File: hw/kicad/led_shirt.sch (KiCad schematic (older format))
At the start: 23 parts, among them J1 10103593-0001LF, P1 icpc, P2 icpd, P3 gnd, P4 v+, P5 mclr, P6 bat+, P7 bat-, P8 led1-, P9 led1+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

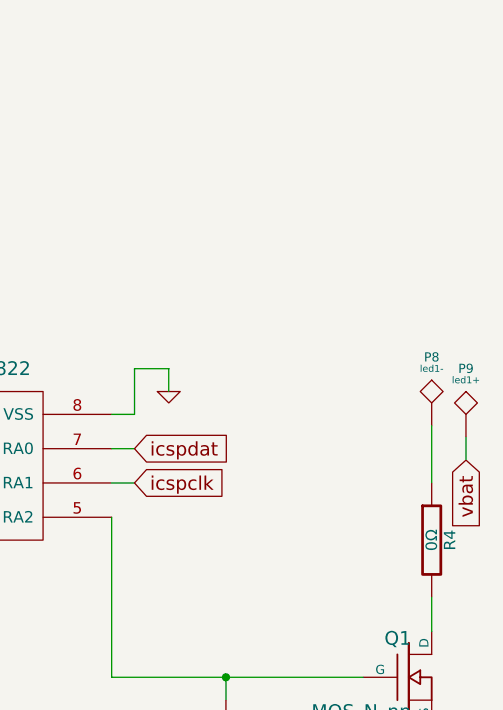
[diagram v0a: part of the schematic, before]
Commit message: add leds to onboard
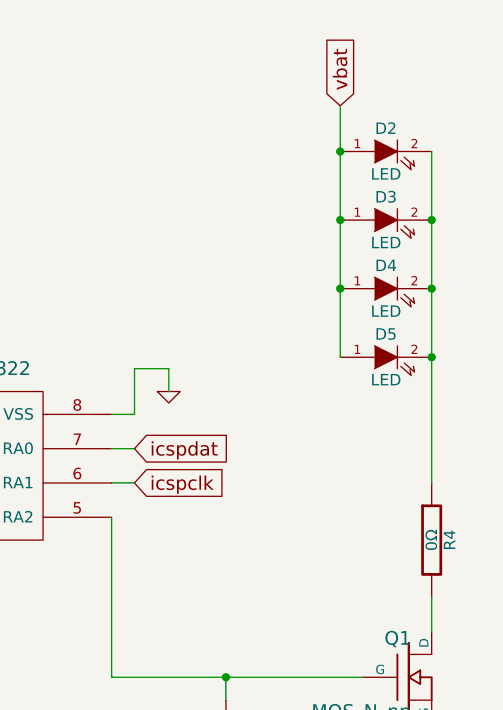
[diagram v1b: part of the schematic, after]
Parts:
- removed P8: led1-, symbol TST
- removed P9: led1+, symbol TST
- added D2, D3, D4, D5: LED, symbol LED
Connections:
- net vbat: now also D2.1 (A), D3.1 (A), D4.1 (A), D5.1 (A)
- net at R4.1: now also D2.2 (K), D3.2 (K), D4.2 (K), D5.2 (K)
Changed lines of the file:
@@
 LIBS:extra
 LIBS:led_shirt-cache
-EELAYER 27 0
+EELAYER 24 0
 EELAYER END
 $Descr A4 11693 8268
@@
 Comment4 ""
 $EndDescr
-Text GLabel 8750 2700 3    60   Input ~ 0
+Text GLabel 8200 1150 1    60   Input ~ 0
 vbat
 $Comp
@@
 	1    0    0    -1
 $EndComp
-$Comp
-L TST P8
-U 1 1 50A3E96A
-P 8600 2550
-F 0 "P8" H 8600 2850 40  0000 C CNN
-F 1 "led1-" H 8600 2800 30  0000 C CNN
-F 2 "" H 8600 2550 60  0001 C CNN
-F 3 "" H 8600 2550 60  0001 C CNN
-	1    8600 2550
-	1    0    0    -1
-$EndComp
 Text GLabel 5450 1900 0    60   Input ~ 0
 vbat
@@
 $EndComp
 $Comp
-L GND #PWR01
+L GND #PWR5
 U 1 1 509FF06B
 P 4650 2700
-F 0 "#PWR01" H 4650 2700 30  0001 C CNN
+F 0 "#PWR5" H 4650 2700 30  0001 C CNN
 F 1 "GND" H 4650 2630 30  0001 C CNN
 F 2 "" H 4650 2700 60  0001 C CNN
@@
 $EndComp
 $Comp
-L TST P9
-U 1 1 509ED371
-P 8750 2600
-F 0 "P9" H 8750 2900 40  0000 C CNN
-F 1 "led1+" H 8750 2850 30  0000 C CNN
-F 2 "" H 8750 2600 60  0001 C CNN
-F 3 "" H 8750 2600 60  0001 C CNN
-	1    8750 2600
-	1    0    0    -1
-$EndComp
-$Comp
 L R R4
 U 1 1 509E9C0F
@@
 $EndComp
 $Comp
-L GND #PWR02
+L GND #PWR2
 U 1 1 509D17CA
 P 2450 3450
-F 0 "#PWR02" H 2450 3450 30  0001 C CNN
+F 0 "#PWR2" H 2450 3450 30  0001 C CNN
 F 1 "GND" H 2450 3380 30  0001 C CNN
 F 2 "" H 2450 3450 60  0001 C CNN
@@
 $EndComp
 $Comp
-L GND #PWR03
+L GND #PWR4
 U 1 1 509D14DE
 P 3250 1650
-F 0 "#PWR03" H 3250 1650 30  0001 C CNN
+F 0 "#PWR4" H 3250 1650 30  0001 C CNN
 F 1 "GND" H 3250 1580 30  0001 C CNN
 F 2 "" H 3250 1650 60  0001 C CNN
@@
 $EndComp
 $Comp
-L GND #PWR04
+L GND #PWR7
 U 1 1 509D02E2
 P 7450 2400
-F 0 "#PWR04" H 7450 2400 30  0001 C CNN
+F 0 "#PWR7" H 7450 2400 30  0001 C CNN
 F 1 "GND" H 7450 2330 30  0001 C CNN
 F 2 "" H 7450 2400 60  0001 C CNN
@@
 vbat
 $Comp
-L GND #PWR05
+L GND #PWR6
 U 1 1 509D029F
 P 4900 6150
-F 0 "#PWR05" H 4900 6150 30  0001 C CNN
+F 0 "#PWR6" H 4900 6150 30  0001 C CNN
 F 1 "GND" H 4900 6080 30  0001 C CNN
 F 2 "" H 4900 6150 60  0001 C CNN
@@
 $EndComp
 $Comp
-L GND #PWR06
+L GND #PWR3
 U 1 1 509D017A
 P 2450 5850
-F 0 "#PWR06" H 2450 5850 30  0001 C CNN
+F 0 "#PWR3" H 2450 5850 30  0001 C CNN
 F 1 "GND" H 2450 5780 30  0001 C CNN
 F 2 "" H 2450 5850 60  0001 C CNN
@@
 vbus
 $Comp
-L GND #PWR07
+L GND #PWR1
 U 1 1 509D0101
 P 1800 1850
-F 0 "#PWR07" H 1800 1850 30  0001 C CNN
+F 0 "#PWR1" H 1800 1850 30  0001 C CNN
 F 1 "GND" H 1800 1780 30  0001 C CNN
 F 2 "" H 1800 1850 60  0001 C CNN
@@
 $EndComp
 $Comp
-L GND #PWR08
+L GND #PWR8
 U 1 1 52607FD1
 P 8150 4500
-F 0 "#PWR08" H 8150 4500 30  0001 C CNN
+F 0 "#PWR8" H 8150 4500 30  0001 C CNN
 F 1 "GND" H 8150 4430 30  0001 C CNN
 F 2 "" H 8150 4500 60  0000 C CNN
@@
 $EndComp
 Wire Wire Line
-	8750 2600 8750 2700
-Wire Wire Line
 	5450 1900 5450 2050
 Wire Wire Line
@@
 Wire Wire Line
 	8600 3450 8600 3300
-Wire Wire Line
-	8600 2550 8600 2800
 Wire Wire Line
 	5350 2650 6000 2650
@@
 	8600 4400 8600 3850
 Connection ~ 8150 4400
+$Comp
+L LED D2
+U 1 1 526D96FC
+P 8400 1350
+F 0 "D2" H 8400 1450 50  0000 C CNN
+F 1 "LED" H 8400 1250 50  0000 C CNN
+F 2 "" H 8400 1350 60  0000 C CNN
+F 3 "" H 8400 1350 60  0000 C CNN
+	1    8400 1350
+	1    0    0    -1
+$EndComp
+$Comp
+L LED D3
+U 1 1 526D9A7A
+P 8400 1650
+F 0 "D3" H 8400 1750 50  0000 C CNN
+F 1 "LED" H 8400 1550 50  0000 C CNN
+F 2 "" H 8400 1650 60  0000 C CNN
+F 3 "" H 8400 1650 60  0000 C CNN
+	1    8400 1650
+	1    0    0    -1
+$EndComp
+$Comp
+L LED D4
+U 1 1 526D9A85
+P 8400 1950
+F 0 "D4" H 8400 2050 50  0000 C CNN
+F 1 "LED" H 8400 1850 50  0000 C CNN
+F 2 "" H 8400 1950 60  0000 C CNN
+F 3 "" H 8400 1950 60  0000 C CNN
+	1    8400 1950
+	1    0    0    -1
+$EndComp
+$Comp
+L LED D5
+U 1 1 526D9A90
+P 8400 2250
+F 0 "D5" H 8400 2350 50  0000 C CNN
+F 1 "LED" H 8400 2150 50  0000 C CNN
+F 2 "" H 8400 2250 60  0000 C CNN
+F 3 "" H 8400 2250 60  0000 C CNN
+	1    8400 2250
+	1    0    0    -1
+$EndComp
+Wire Wire Line
+	8200 1150 8200 2250
+Connection ~ 8200 1350
+Connection ~ 8200 1650
+Connection ~ 8200 1950
+Wire Wire Line
+	8600 1350 8600 2800
+Connection ~ 8600 1650
+Connection ~ 8600 1950
+Connection ~ 8600 2250
 $EndSCHEMATC
